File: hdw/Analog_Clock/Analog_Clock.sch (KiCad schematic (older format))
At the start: 0 parts

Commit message: More sch work
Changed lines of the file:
@@
 $Descr A 11000 8500
 encoding utf-8
-Sheet 1 20
+Sheet 1 21
 Title ""
 Date ""
@@
 S 6300 1360 500  150
 U 5E98CF45
-F0 "Meter0 DAC" 50
-F1 "Meter0_DAC.sch" 50
+F0 "Meter0" 50
+F1 "Meter0.sch" 50
 $EndSheet
 $Sheet
 S 6300 1710 500  150
-U 5E98E7F7
-F0 "Meter1 DAC" 50
-F1 "Meter1_DAC.sch" 50
+U 5F27FE32
+F0 "Meter1" 50
+F1 "Meter1.sch" 50
 $EndSheet
 $Sheet
 S 6300 2060 500  150
-U 5E99007F
-F0 "Meter2 DAC" 50
-F1 "Meter2_DAC.sch" 50
+U 5F280DC7
+F0 "Meter2" 50
+F1 "Meter2.sch" 50
+$EndSheet
+$Sheet
+S 6300 2410 500  150
+U 5F280E04
+F0 "LED Driver" 50
+F1 "LED_Driver.sch" 50
 $EndSheet
 $EndSCHEMATC

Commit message: more sch progress
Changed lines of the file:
@@
 $Descr A 11000 8500
 encoding utf-8
-Sheet 1 21
+Sheet 1 23
 Title ""
 Date ""
@@
 F1 "LED_Driver.sch" 50
 $EndSheet
+$Sheet
+S 6300 2760 500  150
+U 5F28EEB2
+F0 "Pushbuttons" 50
+F1 "Pushbuttons.sch" 50
+$EndSheet
+$Sheet
+S 6300 3110 500  150
+U 5F31BE01
+F0 "Function LEDs" 50
+F1 "Function_LEDs.sch" 50
+$EndSheet
 $EndSCHEMATC

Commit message: more analog work, added some more sch stuff
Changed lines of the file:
@@
 $Descr A 11000 8500
 encoding utf-8
-Sheet 1 23
+Sheet 1 24
 Title ""
 Date ""
@@
 F1 "Function_LEDs.sch" 50
 $EndSheet
+$Sheet
+S 6300 3460 500  150
+U 5F360CB6
+F0 "Misc Circuits" 50
+F1 "Misc_Circuits.sch" 50
+$EndSheet
 $EndSCHEMATC

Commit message: big sch push
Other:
- note removed: "ADD MECH SHEET"
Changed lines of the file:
@@
 $Descr A 11000 8500
 encoding utf-8
-Sheet 1 24
+Sheet 1 25
 Title ""
 Date ""
@@
 F1 "Status_LEDs.sch" 50
 $EndSheet
-Text Notes 6780 6640 0    250  ~ 50
-ADD MECH SHEET
 $Sheet
 S 6300 1360 500  150
@@
 F1 "Misc_Circuits.sch" 50
 $EndSheet
+$Sheet
+S 6300 3810 500  150
+U 5F4453D4
+F0 "Mechanical" 50
+F1 "Mechanical.sch" 50
+$EndSheet
 $EndSCHEMATC

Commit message: Much more schematic progress
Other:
- note added: "01. Table of Contents"
- note added: "02. +12V Input"
- note added: "03. +12V Telemetry"
- note added: "04. +3.3V Power Supply"
- note added: "05. +3.3V Telemetry"
- note added: "06. +20V Power Supply"
- note added: "07. +20V Telemetry"
- note added: "08. PIC32MZ Programming"
- note added: "09. PIC32MZ Bypass"
- note added: "10. PIC32MZ"
- note added: "11. PIC32MZ Clocking"
- note added: "12. Backup RTC"
- note added: "13. USB UART Bridge"
- note added: "14. USB Telemetry"
- note added: "15. Time of Flight"
- note added: "16. PGOOD LEDs"
- note added: "17. Status LEDs"
- note added: "18. Meter0"
- note added: "19. Meter1"
- note added: "20. Meter2"
- note added: "21. LED Driver"
- note added: "22. Pushbuttons"
- note added: "23. Function LEDs"
- note added: "24. Misc Circuits"
- note added: "25. Mechanical"
- note added: "Analog Clock"
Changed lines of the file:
@@
 encoding utf-8
 Sheet 1 25
-Title ""
-Date ""
-Rev ""
-Comp ""
+Title "Analog Clock"
+Date "2020-08-15"
+Rev "A"
+Comp "Drew Maatman"
 Comment1 ""
 Comment2 ""
@@
 $EndSheet
 $Sheet
-S 6300 1360 500  150
+S 7100 1360 500  150
 U 5E98CF45
 F0 "Meter0" 50
@@
 $EndSheet
 $Sheet
-S 6300 1710 500  150
+S 7100 1710 500  150
 U 5F27FE32
 F0 "Meter1" 50
@@
 $EndSheet
 $Sheet
-S 6300 2060 500  150
+S 7100 2060 500  150
 U 5F280DC7
 F0 "Meter2" 50
@@
 $EndSheet
 $Sheet
-S 6300 2410 500  150
+S 7100 2410 500  150
 U 5F280E04
 F0 "LED Driver" 50
@@
 $EndSheet
 $Sheet
-S 6300 2760 500  150
+S 7100 2760 500  150
 U 5F28EEB2
 F0 "Pushbuttons" 50
@@
 $EndSheet
 $Sheet
-S 6300 3110 500  150
+S 7100 3110 500  150
 U 5F31BE01
 F0 "Function LEDs" 50
@@
 $EndSheet
 $Sheet
-S 6300 3460 500  150
+S 7100 3460 500  150
 U 5F360CB6
 F0 "Misc Circuits" 50
@@
 $EndSheet
 $Sheet
-S 6300 3810 500  150
+S 7100 3810 500  150
 U 5F4453D4
 F0 "Mechanical" 50
 F1 "Mechanical.sch" 50
 $EndSheet
+Text Notes 4120 950  0    250  ~ 50
+Analog Clock
+Text Notes 840  1510 0    100  ~ 20
+02. +12V Input
+Text Notes 840  1860 0    100  ~ 20
+03. +12V Telemetry
+Text Notes 840  2210 0    100  ~ 20
+04. +3.3V Power Supply
+Text Notes 840  2560 0    100  ~ 20
+05. +3.3V Telemetry
+Text Notes 840  2910 0    100  ~ 20
+06. +20V Power Supply
+Text Notes 840  3260 0    100  ~ 20
+07. +20V Telemetry
+Text Notes 840  3610 0    100  ~ 20
+08. PIC32MZ Programming
+Text Notes 840  3960 0    100  ~ 20
+09. PIC32MZ Bypass
+Text Notes 840  4310 0    100  ~ 20
+10. PIC32MZ
+Text Notes 840  4660 0    100  ~ 20
+11. PIC32MZ Clocking
+Text Notes 840  5010 0    100  ~ 20
+12. Backup RTC
+Text Notes 840  5360 0    100  ~ 20
+13. USB UART Bridge
+Text Notes 840  5710 0    100  ~ 20
+14. USB Telemetry
+Text Notes 840  6060 0    100  ~ 20
+15. Time of Flight
+Text Notes 840  6410 0    100  ~ 20
+16. PGOOD LEDs
+Text Notes 840  6760 0    100  ~ 20
+17. Status LEDs
+Text Notes 840  1160 0    100  ~ 20
+01. Table of Contents
+Text Notes 5290 1510 0    100  ~ 20
+18. Meter0
+Text Notes 5290 1860 0    100  ~ 20
+19. Meter1
+Text Notes 5290 2210 0    100  ~ 20
+20. Meter2
+Text Notes 5290 2560 0    100  ~ 20
+21. LED Driver
+Text Notes 5290 2910 0    100  ~ 20
+22. Pushbuttons
+Text Notes 5290 3260 0    100  ~ 20
+23. Function LEDs
+Text Notes 5290 3610 0    100  ~ 20
+24. Misc Circuits
+Text Notes 5290 3960 0    100  ~ 20
+25. Mechanical
 $EndSCHEMATC

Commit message: More PCB arrangement
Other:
- note added: "14. (Reserved)"
- note removed: "14. USB Telemetry"
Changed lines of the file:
@@
 $Descr A 11000 8500
 encoding utf-8
-Sheet 1 25
+Sheet 1 24
 Title "Analog Clock"
 Date "2020-08-15"
@@
 F0 "USB UART Bridge" 50
 F1 "USB_Uart_Bridge.sch" 50
-$EndSheet
-$Sheet
-S 3110 5560 500  150
-U 5E939F86
-F0 "USB Telemetry" 50
-F1 "USB_Telemetry.sch" 50
-$EndSheet
-$Sheet
-S 3110 5910 500  150
-U 5E93A1E8
-F0 "Time of Flight" 50
-F1 "Time_of_Flight.sch" 50
-$EndSheet
-$Sheet
-S 3110 6260 500  150
-U 5E93CC4E
-F0 "PGOOD LEDs" 50
-F1 "PGOOD_LEDs.sch" 50
-$EndSheet
-$Sheet
-S 3110 6610 500  150
-U 5E93E000
-F0 "Status LEDs" 50
-F1 "Status_LEDs.sch" 50
 $EndSheet
 $Sheet
@@
 Text Notes 840  5360 0    100  ~ 20
 13. USB UART Bridge
-Text Notes 840  5710 0    100  ~ 20
-14. USB Telemetry
-Text Notes 840  6060 0    100  ~ 20
-15. Time of Flight
-Text Notes 840  6410 0    100  ~ 20
-16. PGOOD LEDs
-Text Notes 840  6760 0    100  ~ 20
-17. Status LEDs
 Text Notes 840  1160 0    100  ~ 20
 01. Table of Contents
@@
 Text Notes 5290 3960 0    100  ~ 20
 25. Mechanical
+Text Notes 840  6760 0    100  ~ 20
+17. Status LEDs
+Text Notes 840  6410 0    100  ~ 20
+16. PGOOD LEDs
+Text Notes 840  6060 0    100  ~ 20
+15. Time of Flight
+$Sheet
+S 3110 6610 500  150
+U 5E93E000
+F0 "Status LEDs" 50
+F1 "Status_LEDs.sch" 50
+$EndSheet
+$Sheet
+S 3110 6260 500  150
+U 5E93CC4E
+F0 "PGOOD LEDs" 50
+F1 "PGOOD_LEDs.sch" 50
+$EndSheet
+$Sheet
+S 3110 5910 500  150
+U 5E93A1E8
+F0 "Time of Flight" 50
+F1 "Time_of_Flight.sch" 50
+$EndSheet
+Text Notes 840  5710 0    100  ~ 20
+14. (Reserved)
 $EndSCHEMATC

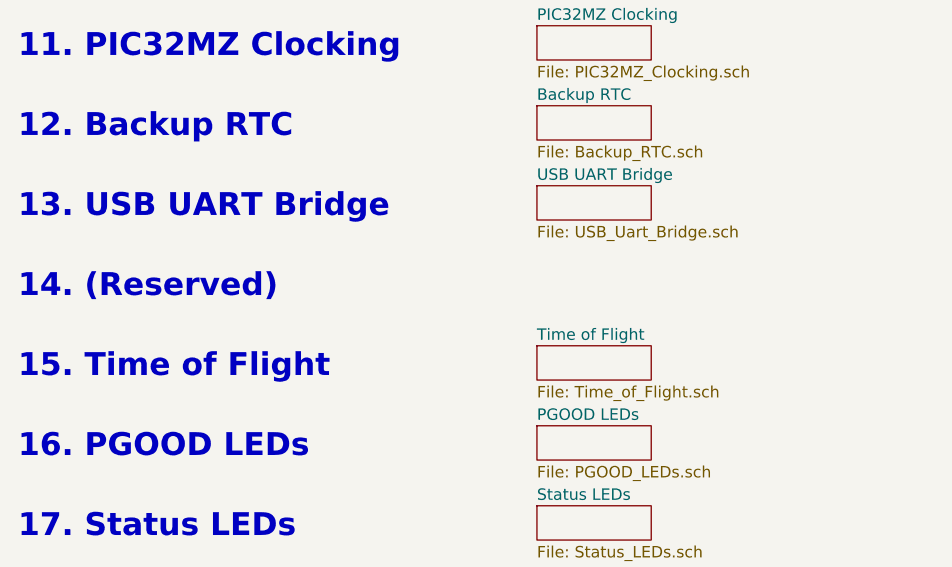
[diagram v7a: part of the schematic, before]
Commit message: Major USB restructuring
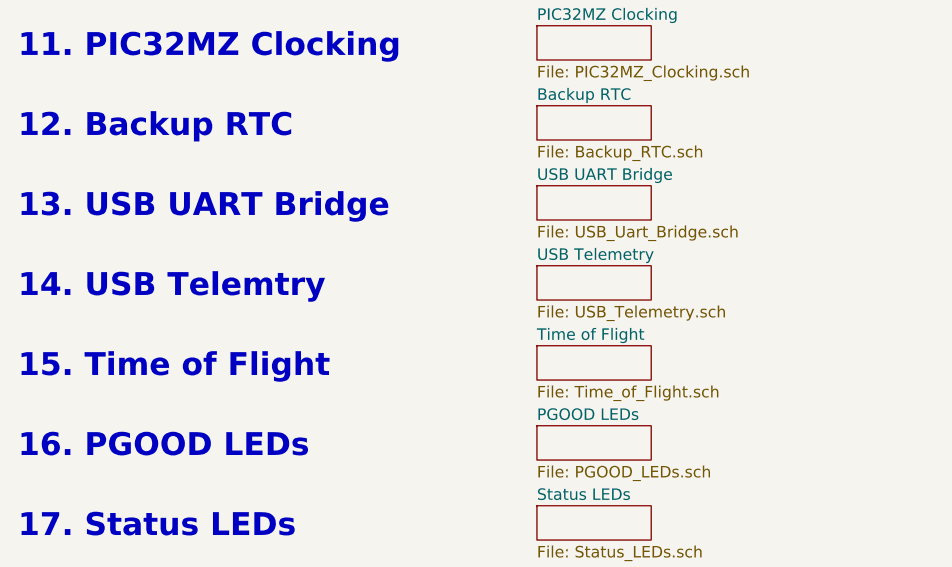
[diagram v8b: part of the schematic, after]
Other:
- note added: "14. USB Telemtry"
- note removed: "14. (Reserved)"
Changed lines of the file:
@@
 $Descr A 11000 8500
 encoding utf-8
-Sheet 1 24
+Sheet 1 25
 Title "Analog Clock"
 Date "2020-08-15"
@@
 F0 "USB UART Bridge" 50
 F1 "USB_Uart_Bridge.sch" 50
+$EndSheet
+$Sheet
+S 3110 5560 500  150
+U 5F6EEAE8
+F0 "USB Telemetry" 50
+F1 "USB_Telemetry.sch" 50
 $EndSheet
 $Sheet
@@
 $EndSheet
 Text Notes 840  5710 0    100  ~ 20
-14. (Reserved)
+14. USB Telemtry
 $EndSCHEMATC
